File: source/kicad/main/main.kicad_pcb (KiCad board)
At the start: 4 copper layers, 50 x 50 mm, 108 parts

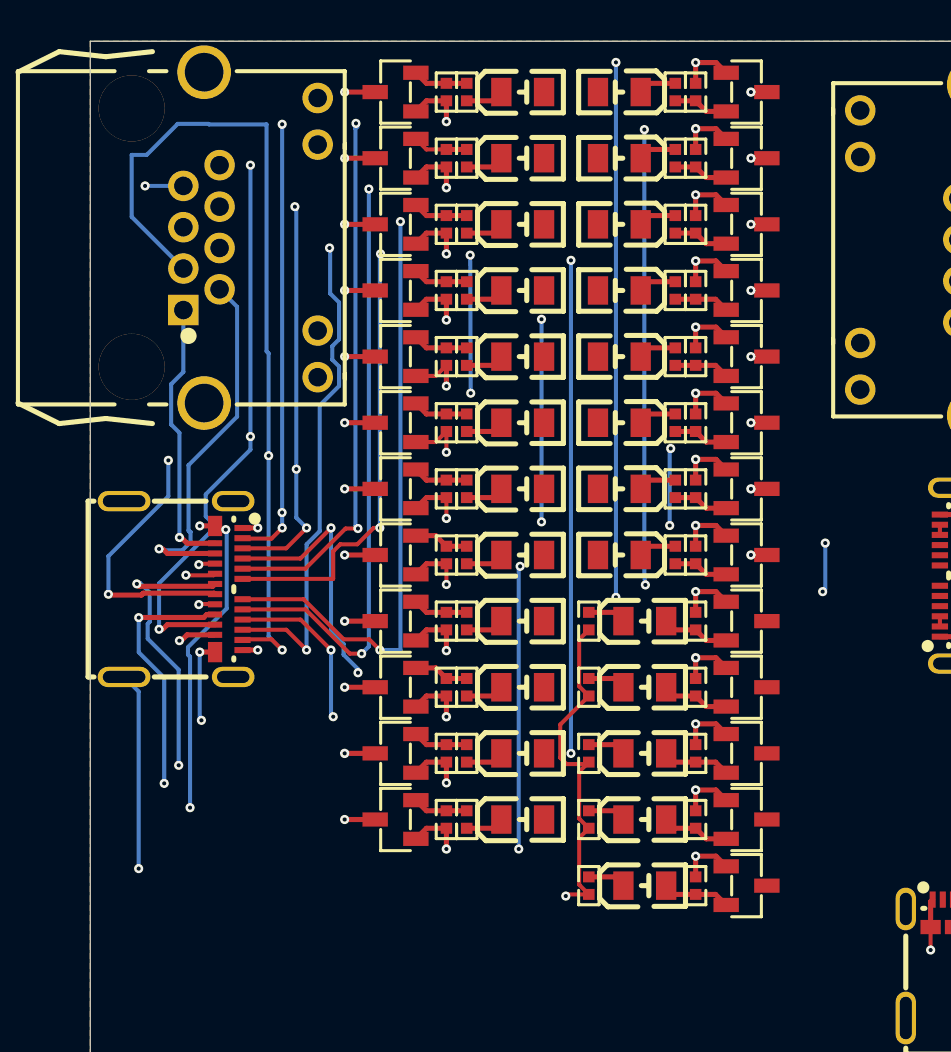
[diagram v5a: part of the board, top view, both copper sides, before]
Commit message: Bugfixes 1.0.0; WIP; Not exported yet.
- Fixed USB-C PD resistors
- Improved part-picking
- Fixed LedIndicator (wrong PowerSwitch usage)
- Reduced LED brightness
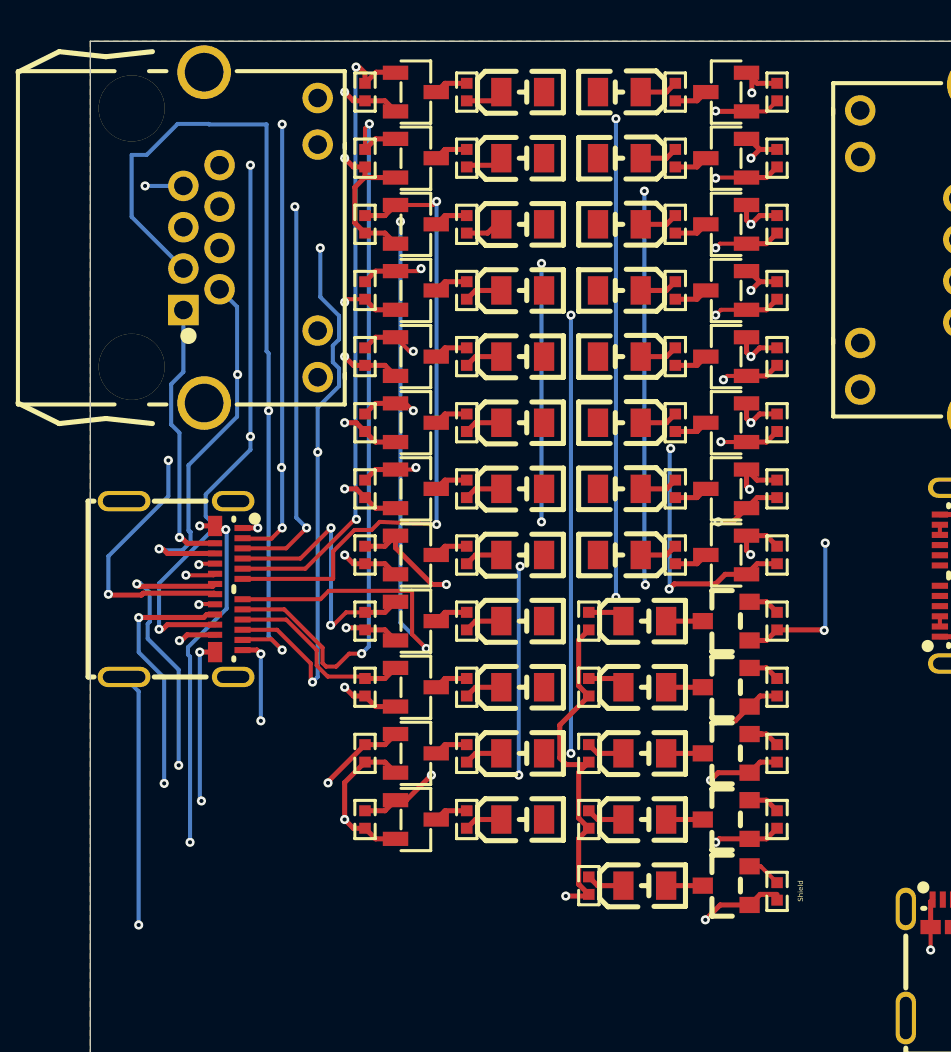
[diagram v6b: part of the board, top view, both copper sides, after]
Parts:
- removed tester.cc1.indicator.led.current_limiting_resistor[Resistor:300Ω], tester.cc2.indicator.led.current_limiting_resistor[Resistor:300Ω], tester.d1[0].indicator.led.current_limiting_resistor[Resistor:300Ω], tester.d1[1].indicator.led.current_limiting_resistor[Resistor:300Ω], tester.d2[0].indicator.led.current_limiting_resistor[Resistor:300Ω], tester.d2[1].indicator.led.current_limiting_resistor[Resistor:300Ω], tester.gnd[0].indicator.led.current_limiting_resistor[Resistor:300Ω], tester.gnd[1].indicator.led.current_limiting_resistor[Resistor:300Ω], tester.gnd[2].indicator.led.current_limiting_resistor[Resistor:300Ω], tester.gnd[3].indicator.led.current_limiting_resistor[Resistor:300Ω], tester.pair1_rx1[0].indicator.led.current_limiting_resistor[Resistor:300Ω], tester.pair1_rx1[1].indicator.led.current_limiting_resistor[Resistor:300Ω], tester.pair2_rx2[0].indicator.led.current_limiting_resistor[Resistor:300Ω], tester.pair2_rx2[1].indicator.led.current_limiting_resistor[Resistor:300Ω], tester.pair3_tx1[0].indicator.led.current_limiting_resistor[Resistor:300Ω], tester.pair3_tx1[1].indicator.led.current_limiting_resistor[Resistor:300Ω], tester.pair4_tx2[0].indicator.led.current_limiting_resistor[Resistor:300Ω], tester.pair4_tx2[1].indicator.led.current_limiting_resistor[Resistor:300Ω], tester.sbu1.indicator.led.current_limiting_resistor[Resistor:300Ω], tester.sbu2.indicator.led.current_limiting_resistor[Resistor:300Ω], tester.shield.indicator.led.current_limiting_resistor[Resistor:300Ω], tester.vbus[0].indicator.led.current_limiting_resistor[Resistor:300Ω], tester.vbus[1].indicator.led.current_limiting_resistor[Resistor:300Ω], tester.vbus[2].indicator.led.current_limiting_resistor[Resistor:300Ω], tester.vbus[3].indicator.led.current_limiting_resistor[Resistor:300Ω]: 300Ω, lcsc:R0402
- added tester.cc1.indicator.led.current_limiting_resistor[Resistor:1KΩ]: 1KΩ, lcsc:R0402, F.Cu at (18.5, 2.50)
- added tester.cc2.indicator.led.current_limiting_resistor[Resistor:1KΩ]: 1KΩ, lcsc:R0402, F.Cu at (28.8, 2.50)
- added tester.d1[0].indicator.led.current_limiting_resistor[Resistor:1KΩ]: 1KΩ, lcsc:R0402, F.Cu at (18.5, 9.00)
- added tester.d1[1].indicator.led.current_limiting_resistor[Resistor:1KΩ]: 1KΩ, lcsc:R0402, F.Cu at (28.8, 9.00)
- added tester.d2[0].indicator.led.current_limiting_resistor[Resistor:1KΩ]: 1KΩ, lcsc:R0402, F.Cu at (18.5, 12.2)
- added tester.d2[1].indicator.led.current_limiting_resistor[Resistor:1KΩ]: 1KΩ, lcsc:R0402, F.Cu at (28.8, 12.2)
- added tester.gnd[0].indicator.led.current_limiting_resistor[Resistor:1KΩ]: 1KΩ, lcsc:R0402, F.Cu at (24.5, 28.5)
- added tester.gnd[1].indicator.led.current_limiting_resistor[Resistor:1KΩ]: 1KΩ, lcsc:R0402, F.Cu at (24.5, 31.8)
- added tester.gnd[2].indicator.led.current_limiting_resistor[Resistor:1KΩ]: 1KΩ, lcsc:R0402, F.Cu at (24.5, 35.0)
- added tester.gnd[3].indicator.led.current_limiting_resistor[Resistor:1KΩ]: 1KΩ, lcsc:R0402, F.Cu at (24.5, 38.2)
- added tester.pair1_rx1[0].indicator.led.current_limiting_resistor[Resistor:1KΩ]: 1KΩ, lcsc:R0402, F.Cu at (18.5, 15.5)
- added tester.pair1_rx1[1].indicator.led.current_limiting_resistor[Resistor:1KΩ]: 1KΩ, lcsc:R0402, F.Cu at (28.8, 15.5)
- added tester.pair2_rx2[0].indicator.led.current_limiting_resistor[Resistor:1KΩ]: 1KΩ, lcsc:R0402, F.Cu at (18.5, 18.8)
- added tester.pair2_rx2[1].indicator.led.current_limiting_resistor[Resistor:1KΩ]: 1KΩ, lcsc:R0402, F.Cu at (28.8, 18.8)
- added tester.pair3_tx1[0].indicator.led.current_limiting_resistor[Resistor:1KΩ]: 1KΩ, lcsc:R0402, F.Cu at (18.5, 22.0)
- added tester.pair3_tx1[1].indicator.led.current_limiting_resistor[Resistor:1KΩ]: 1KΩ, lcsc:R0402, F.Cu at (28.8, 22.0)
- added tester.pair4_tx2[0].indicator.led.current_limiting_resistor[Resistor:1KΩ]: 1KΩ, lcsc:R0402, F.Cu at (18.5, 25.2)
- added tester.pair4_tx2[1].indicator.led.current_limiting_resistor[Resistor:1KΩ]: 1KΩ, lcsc:R0402, F.Cu at (28.8, 25.2)
- added tester.sbu1.indicator.led.current_limiting_resistor[Resistor:1KΩ]: 1KΩ, lcsc:R0402, F.Cu at (18.5, 5.75)
- added tester.sbu2.indicator.led.current_limiting_resistor[Resistor:1KΩ]: 1KΩ, lcsc:R0402, F.Cu at (28.8, 5.75)
- added tester.shield.indicator.led.current_limiting_resistor[Resistor:1KΩ]: 1KΩ, lcsc:R0402, F.Cu at (24.5, 41.5)
- added tester.vbus[0].indicator.led.current_limiting_resistor[Resistor:1KΩ]: 1KΩ, lcsc:R0402, F.Cu at (18.5, 28.5)
- added tester.vbus[1].indicator.led.current_limiting_resistor[Resistor:1KΩ]: 1KΩ, lcsc:R0402, F.Cu at (18.5, 31.8)
- added tester.vbus[2].indicator.led.current_limiting_resistor[Resistor:1KΩ]: 1KΩ, lcsc:R0402, F.Cu at (18.5, 35.0)
- added tester.vbus[3].indicator.led.current_limiting_resistor[Resistor:1KΩ]: 1KΩ, lcsc:R0402, F.Cu at (18.5, 38.2)
- tester.gnd[0].indicator.power_switch.mosfet[MOSFET:Q], tester.gnd[1].indicator.power_switch.mosfet[MOSFET:Q], tester.gnd[2].indicator.power_switch.mosfet[MOSFET:Q], tester.gnd[3].indicator.power_switch.mosfet[MOSFET:Q], tester.shield.indicator.power_switch.mosfet[MOSFET:Q]: footprint lcsc:SOT-23-3_L2.9-W1.3-P1.90-LS2.4-BR -> lcsc:SOT-23_L2.9-W1.3-P1.90-LS2.4-BR
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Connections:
- net psu.usb[USB_C_Receptacle:x]-psu.configuration_resistors[1][Resistor:5.0KΩ] renamed psu.configuration_resistors[1][Resistor:5.0KΩ]-psu.usb[USB_C_Receptacle:x]
- net tester.d1[0].indicator.power_switch[PowerSwitch:virt]-tester.d1[0][PairTester:virt]:4-tester.d1[0].i renamed tester.d1[0].indicator[LEDIndicator:virt]-tester.d1[0].indicator.power_switch[PowerSwitch:virt]-test
- net tester.d1[1].indicator.power_switch[PowerSwitch:virt]-tester.d1[1].indicator[LEDIndicator:virt]-test renamed tester.d1[1].indicator.power_switch[PowerSwitch:virt]-tester.d1[1][PairTester:virt]:4-tester.d1[1].i
- net tester.d2[0][PairTester:virt]:4-tester.d2[0].indicator.power_switch[PowerSwitch:virt]-tester.d2[0].i renamed tester.d2[0][PairTester:virt]:4-tester.d2[0].indicator[LEDIndicator:virt]-tester.d2[0].indicator.pow
- net tester.d2[1].indicator.power_switch[PowerSwitch:virt]-tester.d2[1][PairTester:virt]:4-tester.d2[1].i renamed tester.d2[1].indicator.power_switch[PowerSwitch:virt]-tester.d2[1].indicator[LEDIndicator:virt]-test
- net tester.gnd[0].indicator[LEDIndicator:virt]-tester.gnd[0][PairTester:virt]:4-tester.gnd[0].indicator. renamed tester.gnd[0][PairTester:virt]:4-tester.gnd[0].indicator[LEDIndicator:virt]-tester.gnd[0].indicator.
- net tester.gnd[1].indicator[LEDIndicator:virt]-tester.gnd[1][PairTester:virt]:4-tester.gnd[1].indicator. renamed tester.gnd[1][PairTester:virt]:4-tester.gnd[1].indicator.power_switch[PowerSwitch:virt]-tester.gnd[1
- net tester.gnd[2].indicator[LEDIndicator:virt]-tester.gnd[2][PairTester:virt]:4-tester.gnd[2].indicator. renamed tester.gnd[2][PairTester:virt]:4-tester.gnd[2].indicator.power_switch[PowerSwitch:virt]-tester.gnd[2
- net tester.gnd[3][PairTester:virt]:4-tester.gnd[3].indicator[LEDIndicator:virt]-tester.gnd[3].indicator. renamed tester.gnd[3][PairTester:virt]:4-tester.gnd[3].indicator.power_switch[PowerSwitch:virt]-tester.gnd[3
- net tester.pair2_rx2[0].indicator.power_switch[PowerSwitch:virt]-tester.pair2_rx2[0].indicator[LEDIndica renamed tester.pair2_rx2[0].indicator[LEDIndicator:virt]-tester.pair2_rx2[0].indicator.power_switch[PowerSwi
- net tester.pair3_tx1[0].indicator[LEDIndicator:virt]-tester.pair3_tx1[0][PairTester:virt]:4-tester.pair3 renamed tester.pair3_tx1[0].indicator[LEDIndicator:virt]-tester.pair3_tx1[0].indicator.power_switch[PowerSwi
- net tester.pair3_tx1[1].indicator[LEDIndicator:virt]-tester.pair3_tx1[1][PairTester:virt]:4-tester.pair3 renamed tester.pair3_tx1[1].indicator.power_switch[PowerSwitch:virt]-tester.pair3_tx1[1].indicator[LEDIndica
- net tester.pair4_tx2[0].indicator.power_switch[PowerSwitch:virt]-tester.pair4_tx2[0].indicator[LEDIndica renamed tester.pair4_tx2[0].indicator[LEDIndicator:virt]-tester.pair4_tx2[0][PairTester:virt]:4-tester.pair4
- net tester.pair4_tx2[1][PairTester:virt]:4-tester.pair4_tx2[1].indicator[LEDIndicator:virt]-tester.pair4 renamed tester.pair4_tx2[1].indicator[LEDIndicator:virt]-tester.pair4_tx2[1].indicator.power_switch[PowerSwi
- net tester.sbu1.indicator[LEDIndicator:virt]-tester.sbu1.indicator.power_switch[PowerSwitch:virt]-tester renamed tester.sbu1[PairTester:virt]:4-tester.sbu1.indicator[LEDIndicator:virt]-tester.sbu1.indicator.power_
- net tester.shield[PairTester:virt]:4-tester.shield.indicator[LEDIndicator:virt]-tester.shield.indicator. renamed tester.shield.indicator.power_switch[PowerSwitch:virt]-tester.shield[PairTester:virt]:4-tester.shiel
- net tester.vbus[0].indicator[LEDIndicator:virt]-tester.vbus[0][PairTester:virt]:4-tester.vbus[0].indicat renamed tester.vbus[0][PairTester:virt]:4-tester.vbus[0].indicator.power_switch[PowerSwitch:virt]-tester.vbu
- net tester.vbus[1].indicator.power_switch[PowerSwitch:virt]-tester.vbus[1][PairTester:virt]:4-tester.vbu renamed tester.vbus[1][PairTester:virt]:4-tester.vbus[1].indicator[LEDIndicator:virt]-tester.vbus[1].indicat
- net tester.vbus[3][PairTester:virt]:4-tester.vbus[3].indicator.power_switch[PowerSwitch:virt]-tester.vbu renamed tester.vbus[3].indicator[LEDIndicator:virt]-tester.vbus[3].indicator.power_switch[PowerSwitch:virt]-
- psu.configuration_resistors[0][Resistor:5.0KΩ] pad 2: tester.pair1_rx1[1][PairTester:virt]:2-tester.cc1[PairTester:virt]:2-tester.gnd[0].indicator.power_s -> tester.pair1_rx1[0][PairTester:virt]:2-tester.d1[1].indicator[LEDIndicator:virt]:3-tester.sbu2.indic
- psu.configuration_resistors[1][Resistor:5.0KΩ] pad 2: tester.pair1_rx1[1][PairTester:virt]:2-tester.cc1[PairTester:virt]:2-tester.gnd[0].indicator.power_s -> tester.pair1_rx1[0][PairTester:virt]:2-tester.d1[1].indicator[LEDIndicator:virt]:3-tester.sbu2.indic
- psu.usb[USB_C_Receptacle:x] pad A1: tester.pair1_rx1[1][PairTester:virt]:2-tester.cc1[PairTester:virt]:2-tester.gnd[0].indicator.power_s -> tester.pair1_rx1[0][PairTester:virt]:2-tester.d1[1].indicator[LEDIndicator:virt]:3-tester.sbu2.indic
- psu.usb[USB_C_Receptacle:x] pad A12: tester.pair1_rx1[1][PairTester:virt]:2-tester.cc1[PairTester:virt]:2-tester.gnd[0].indicator.power_s -> tester.pair1_rx1[0][PairTester:virt]:2-tester.d1[1].indicator[LEDIndicator:virt]:3-tester.sbu2.indic
- psu.usb[USB_C_Receptacle:x] pad A4: tester.d1[1].indicator.power_switch[PowerSwitch:virt]:4-tester.pair1_rx1[0].indicator.power_switch[P -> tester.shield.indicator.power_switch[PowerSwitch:virt]:2-tester.d1[1].indicator.power_switch[PowerSw
- psu.usb[USB_C_Receptacle:x] pad A9: tester.d1[1].indicator.power_switch[PowerSwitch:virt]:4-tester.pair1_rx1[0].indicator.power_switch[P -> tester.shield.indicator.power_switch[PowerSwitch:virt]:2-tester.d1[1].indicator.power_switch[PowerSw
- psu.usb[USB_C_Receptacle:x] pad B1: tester.pair1_rx1[1][PairTester:virt]:2-tester.cc1[PairTester:virt]:2-tester.gnd[0].indicator.power_s -> tester.pair1_rx1[0][PairTester:virt]:2-tester.d1[1].indicator[LEDIndicator:virt]:3-tester.sbu2.indic
- psu.usb[USB_C_Receptacle:x] pad B12: tester.pair1_rx1[1][PairTester:virt]:2-tester.cc1[PairTester:virt]:2-tester.gnd[0].indicator.power_s -> tester.pair1_rx1[0][PairTester:virt]:2-tester.d1[1].indicator[LEDIndicator:virt]:3-tester.sbu2.indic
- psu.usb[USB_C_Receptacle:x] pad B4: tester.d1[1].indicator.power_switch[PowerSwitch:virt]:4-tester.pair1_rx1[0].indicator.power_switch[P -> tester.shield.indicator.power_switch[PowerSwitch:virt]:2-tester.d1[1].indicator.power_switch[PowerSw
- psu.usb[USB_C_Receptacle:x] pad B9: tester.d1[1].indicator.power_switch[PowerSwitch:virt]:4-tester.pair1_rx1[0].indicator.power_switch[P -> tester.shield.indicator.power_switch[PowerSwitch:virt]:2-tester.d1[1].indicator.power_switch[PowerSw
- tester.cc1.indicator.led.led[LED:D] pad 1: tester.d1[1].indicator.power_switch[PowerSwitch:virt]:4-tester.pair1_rx1[0].indicator.power_switch[P -> tester.shield.indicator.power_switch[PowerSwitch:virt]:2-tester.d1[1].indicator.power_switch[PowerSw
- tester.cc1.indicator.led.led[LED:D] pad 2: tester.cc1.indicator.led.led[LED:D]-tester.cc1.indicator.led.current_limiting_resistor[Resistor:300Ω] -> tester.cc1.indicator.led.current_limiting_resistor[Resistor:1KΩ]-tester.cc1.indicator.led.led[LED:D]
- tester.cc1.indicator.power_switch.mosfet[MOSFET:Q] pad 2: tester.cc1.indicator.led[PoweredLED:virt]:2-tester.cc1.indicator.power_switch[PowerSwitch:virt]:3 -> tester.pair1_rx1[0][PairTester:virt]:2-tester.d1[1].indicator[LEDIndicator:virt]:3-tester.sbu2.indic
- tester.cc1.indicator.power_switch.mosfet[MOSFET:Q] pad 3: tester.pair1_rx1[1][PairTester:virt]:2-tester.cc1[PairTester:virt]:2-tester.gnd[0].indicator.power_s -> tester.cc1.indicator.led[PoweredLED:virt]:2-tester.cc1.indicator.power_switch[PowerSwitch:virt]:5
- tester.cc1.indicator.power_switch.pull_resistor[Resistor:100KΩ] pad 2: tester.cc1.indicator.led[PoweredLED:virt]:2-tester.cc1.indicator.power_switch[PowerSwitch:virt]:3 -> tester.pair1_rx1[0][PairTester:virt]:2-tester.d1[1].indicator[LEDIndicator:virt]:3-tester.sbu2.indic
- tester.cc2.indicator.led.led[LED:D] pad 1: tester.d1[1].indicator.power_switch[PowerSwitch:virt]:4-tester.pair1_rx1[0].indicator.power_switch[P -> tester.shield.indicator.power_switch[PowerSwitch:virt]:2-tester.d1[1].indicator.power_switch[PowerSw
- tester.cc2.indicator.led.led[LED:D] pad 2: tester.cc2.indicator.led.current_limiting_resistor[Resistor:300Ω]-tester.cc2.indicator.led.led[LED:D] -> tester.cc2.indicator.led.current_limiting_resistor[Resistor:1KΩ]-tester.cc2.indicator.led.led[LED:D]
- tester.cc2.indicator.power_switch.mosfet[MOSFET:Q] pad 2: tester.cc2.indicator.power_switch[PowerSwitch:virt]:3-tester.cc2.indicator.led[PoweredLED:virt]:2 -> tester.pair1_rx1[0][PairTester:virt]:2-tester.d1[1].indicator[LEDIndicator:virt]:3-tester.sbu2.indic
- tester.cc2.indicator.power_switch.mosfet[MOSFET:Q] pad 3: tester.pair1_rx1[1][PairTester:virt]:2-tester.cc1[PairTester:virt]:2-tester.gnd[0].indicator.power_s -> tester.cc2.indicator.led[PoweredLED:virt]:2-tester.cc2.indicator.power_switch[PowerSwitch:virt]:5
- tester.cc2.indicator.power_switch.pull_resistor[Resistor:100KΩ] pad 2: tester.cc2.indicator.power_switch[PowerSwitch:virt]:3-tester.cc2.indicator.led[PoweredLED:virt]:2 -> tester.pair1_rx1[0][PairTester:virt]:2-tester.d1[1].indicator[LEDIndicator:virt]:3-tester.sbu2.indic
- tester.d1[0].indicator.led.led[LED:D] pad 1: tester.d1[1].indicator.power_switch[PowerSwitch:virt]:4-tester.pair1_rx1[0].indicator.power_switch[P -> tester.shield.indicator.power_switch[PowerSwitch:virt]:2-tester.d1[1].indicator.power_switch[PowerSw
- tester.d1[0].indicator.led.led[LED:D] pad 2: tester.d1[0].indicator.led.led[LED:D]-tester.d1[0].indicator.led.current_limiting_resistor[Resistor:300Ω] -> tester.d1[0].indicator.led.led[LED:D]-tester.d1[0].indicator.led.current_limiting_resistor[Resistor:1KΩ]
- tester.d1[0].indicator.power_switch.mosfet[MOSFET:Q] pad 2: tester.d1[0].indicator.led[PoweredLED:virt]:2-tester.d1[0].indicator.power_switch[PowerSwitch:virt]: -> tester.pair1_rx1[0][PairTester:virt]:2-tester.d1[1].indicator[LEDIndicator:virt]:3-tester.sbu2.indic
- tester.d1[0].indicator.power_switch.mosfet[MOSFET:Q] pad 3: tester.pair1_rx1[1][PairTester:virt]:2-tester.cc1[PairTester:virt]:2-tester.gnd[0].indicator.power_s -> tester.d1[0].indicator.power_switch[PowerSwitch:virt]:5-tester.d1[0].indicator.led[PoweredLED:virt]:
- tester.d1[0].indicator.power_switch.pull_resistor[Resistor:100KΩ] pad 2: tester.d1[0].indicator.led[PoweredLED:virt]:2-tester.d1[0].indicator.power_switch[PowerSwitch:virt]: -> tester.pair1_rx1[0][PairTester:virt]:2-tester.d1[1].indicator[LEDIndicator:virt]:3-tester.sbu2.indic
- tester.d1[1].indicator.led.led[LED:D] pad 1: tester.d1[1].indicator.power_switch[PowerSwitch:virt]:4-tester.pair1_rx1[0].indicator.power_switch[P -> tester.shield.indicator.power_switch[PowerSwitch:virt]:2-tester.d1[1].indicator.power_switch[PowerSw
- tester.d1[1].indicator.led.led[LED:D] pad 2: tester.d1[1].indicator.led.current_limiting_resistor[Resistor:300Ω]-tester.d1[1].indicator.led.led[LED:D] -> tester.d1[1].indicator.led.current_limiting_resistor[Resistor:1KΩ]-tester.d1[1].indicator.led.led[LED:D]
- tester.d1[1].indicator.power_switch.mosfet[MOSFET:Q] pad 2: tester.d1[1].indicator.led[PoweredLED:virt]:2-tester.d1[1].indicator.power_switch[PowerSwitch:virt]: -> tester.pair1_rx1[0][PairTester:virt]:2-tester.d1[1].indicator[LEDIndicator:virt]:3-tester.sbu2.indic
- tester.d1[1].indicator.power_switch.mosfet[MOSFET:Q] pad 3: tester.pair1_rx1[1][PairTester:virt]:2-tester.cc1[PairTester:virt]:2-tester.gnd[0].indicator.power_s -> tester.d1[1].indicator.power_switch[PowerSwitch:virt]:5-tester.d1[1].indicator.led[PoweredLED:virt]:
- tester.d1[1].indicator.power_switch.pull_resistor[Resistor:100KΩ] pad 2: tester.d1[1].indicator.led[PoweredLED:virt]:2-tester.d1[1].indicator.power_switch[PowerSwitch:virt]: -> tester.pair1_rx1[0][PairTester:virt]:2-tester.d1[1].indicator[LEDIndicator:virt]:3-tester.sbu2.indic
- tester.d2[0].indicator.led.led[LED:D] pad 1: tester.d1[1].indicator.power_switch[PowerSwitch:virt]:4-tester.pair1_rx1[0].indicator.power_switch[P -> tester.shield.indicator.power_switch[PowerSwitch:virt]:2-tester.d1[1].indicator.power_switch[PowerSw
- tester.d2[0].indicator.led.led[LED:D] pad 2: tester.d2[0].indicator.led.current_limiting_resistor[Resistor:300Ω]-tester.d2[0].indicator.led.led[LED:D] -> tester.d2[0].indicator.led.led[LED:D]-tester.d2[0].indicator.led.current_limiting_resistor[Resistor:1KΩ]
- tester.d2[0].indicator.power_switch.mosfet[MOSFET:Q] pad 2: tester.d2[0].indicator.led[PoweredLED:virt]:2-tester.d2[0].indicator.power_switch[PowerSwitch:virt]: -> tester.pair1_rx1[0][PairTester:virt]:2-tester.d1[1].indicator[LEDIndicator:virt]:3-tester.sbu2.indic
- tester.d2[0].indicator.power_switch.mosfet[MOSFET:Q] pad 3: tester.pair1_rx1[1][PairTester:virt]:2-tester.cc1[PairTester:virt]:2-tester.gnd[0].indicator.power_s -> tester.d2[0].indicator.led[PoweredLED:virt]:2-tester.d2[0].indicator.power_switch[PowerSwitch:virt]:
- tester.d2[0].indicator.power_switch.pull_resistor[Resistor:100KΩ] pad 2: tester.d2[0].indicator.led[PoweredLED:virt]:2-tester.d2[0].indicator.power_switch[PowerSwitch:virt]: -> tester.pair1_rx1[0][PairTester:virt]:2-tester.d1[1].indicator[LEDIndicator:virt]:3-tester.sbu2.indic
- tester.d2[1].indicator.led.led[LED:D] pad 1: tester.d1[1].indicator.power_switch[PowerSwitch:virt]:4-tester.pair1_rx1[0].indicator.power_switch[P -> tester.shield.indicator.power_switch[PowerSwitch:virt]:2-tester.d1[1].indicator.power_switch[PowerSw
- tester.d2[1].indicator.led.led[LED:D] pad 2: tester.d2[1].indicator.led.current_limiting_resistor[Resistor:300Ω]-tester.d2[1].indicator.led.led[LED:D] -> tester.d2[1].indicator.led.current_limiting_resistor[Resistor:1KΩ]-tester.d2[1].indicator.led.led[LED:D]
- tester.d2[1].indicator.power_switch.mosfet[MOSFET:Q] pad 2: tester.d2[1].indicator.led[PoweredLED:virt]:2-tester.d2[1].indicator.power_switch[PowerSwitch:virt]: -> tester.pair1_rx1[0][PairTester:virt]:2-tester.d1[1].indicator[LEDIndicator:virt]:3-tester.sbu2.indic
- tester.d2[1].indicator.power_switch.mosfet[MOSFET:Q] pad 3: tester.pair1_rx1[1][PairTester:virt]:2-tester.cc1[PairTester:virt]:2-tester.gnd[0].indicator.power_s -> tester.d2[1].indicator.led[PoweredLED:virt]:2-tester.d2[1].indicator.power_switch[PowerSwitch:virt]:
- tester.d2[1].indicator.power_switch.pull_resistor[Resistor:100KΩ] pad 2: tester.d2[1].indicator.led[PoweredLED:virt]:2-tester.d2[1].indicator.power_switch[PowerSwitch:virt]: -> tester.pair1_rx1[0][PairTester:virt]:2-tester.d1[1].indicator[LEDIndicator:virt]:3-tester.sbu2.indic
- tester.gnd[0].indicator.led.led[LED:D] pad 2: tester.gnd[0].indicator.led.led[LED:D]-tester.gnd[0].indicator.led.current_limiting_resistor[Resistor:300Ω] -> tester.gnd[0].indicator.led.current_limiting_resistor[Resistor:1KΩ]-tester.gnd[0].indicator.led.led[LED:D]
- tester.gnd[0].indicator.power_switch.mosfet[MOSFET:Q] pad 2: tester.gnd[0].indicator.led[PoweredLED:virt]-tester.gnd[0].indicator.power_switch[PowerSwitch:virt]: -> tester.shield.indicator.power_switch[PowerSwitch:virt]:2-tester.d1[1].indicator.power_switch[PowerSw
- tester.gnd[0].indicator.power_switch.mosfet[MOSFET:Q] pad 3: tester.d1[1].indicator.power_switch[PowerSwitch:virt]:4-tester.pair1_rx1[0].indicator.power_switch[P -> tester.gnd[0].indicator.led[PoweredLED:virt]-tester.gnd[0].indicator.power_switch[PowerSwitch:virt]:
- tester.gnd[0].indicator.power_switch.pull_resistor[Resistor:100KΩ] pad 2: tester.gnd[0].indicator.led[PoweredLED:virt]-tester.gnd[0].indicator.power_switch[PowerSwitch:virt]: -> tester.shield.indicator.power_switch[PowerSwitch:virt]:2-tester.d1[1].indicator.power_switch[PowerSw
- tester.gnd[1].indicator.led.led[LED:D] pad 1: tester.gnd[1].indicator.power_switch[PowerSwitch:virt]:2-tester.gnd[1].indicator.led[PoweredLED:virt -> tester.gnd[1].indicator.led[PoweredLED:virt]-tester.gnd[1].indicator.power_switch[PowerSwitch:virt]:
- tester.gnd[1].indicator.led.led[LED:D] pad 2: tester.gnd[1].indicator.led.current_limiting_resistor[Resistor:300Ω]-tester.gnd[1].indicator.led.led[LED:D] -> tester.gnd[1].indicator.led.led[LED:D]-tester.gnd[1].indicator.led.current_limiting_resistor[Resistor:1KΩ]
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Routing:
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- added copper zone on F.Cu, net tester.shield.indicator.power_switch[PowerSwitch:virt]:2-tester.d1[1].indicator.power_switch[PowerSw
- removed copper zone on F.Cu, net tester.d1[1].indicator.power_switch[PowerSwitch:virt]:4-tester.pair1_rx1[0].indicator.power_switch[P
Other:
- board text added: "Shield"
- board text added: "USB-C CableTester v1.0.1 https://github.com/IoannisP-ITENG/CableTester"
- board text removed: "USB-C CableTester v1.0.0 https://github.com/IoannisP-ITENG/CableTester"

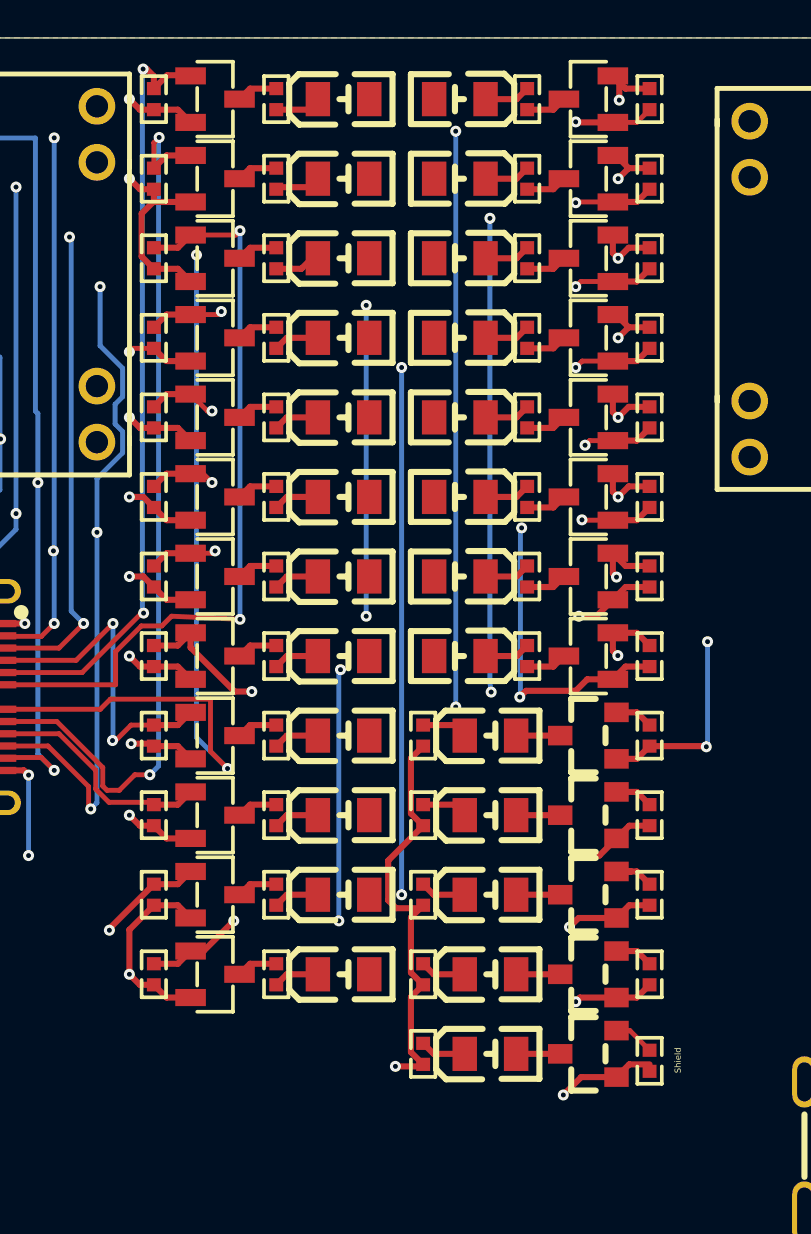
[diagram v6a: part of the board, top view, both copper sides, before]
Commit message: Fix footprints/3dmodels
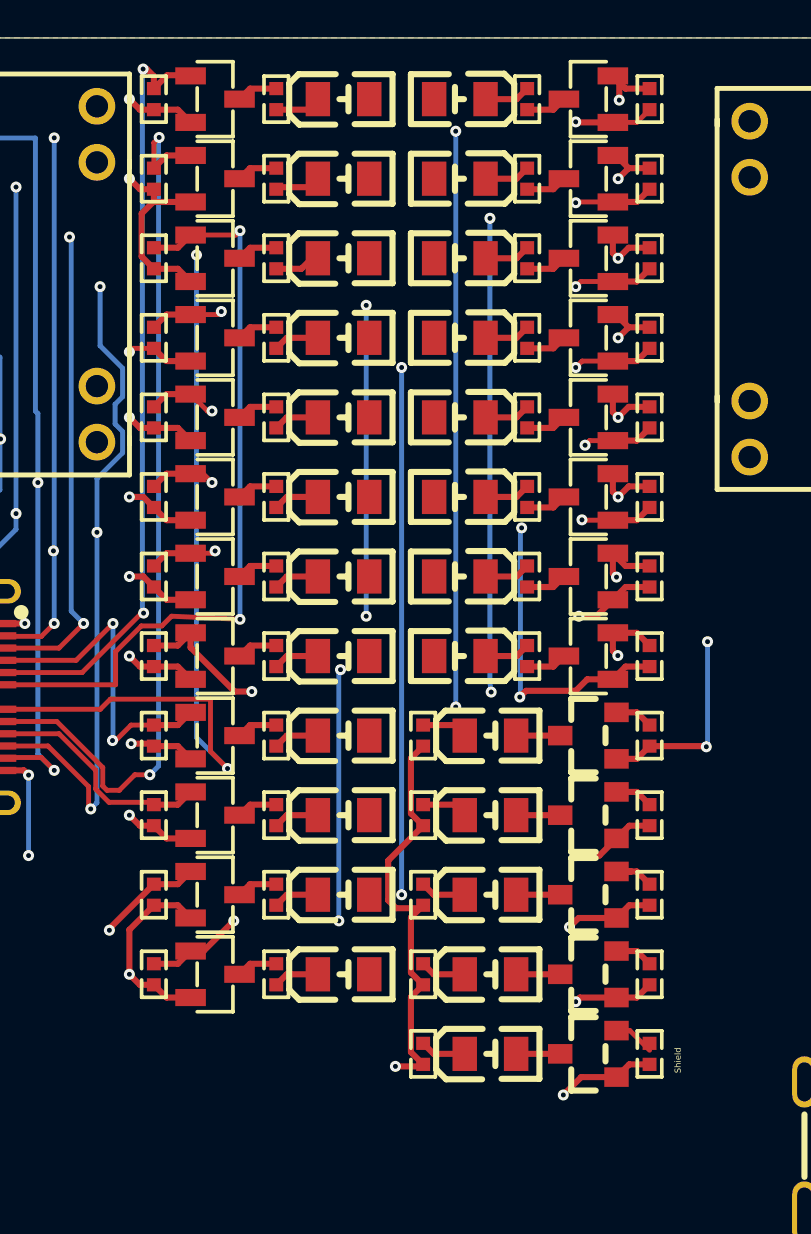
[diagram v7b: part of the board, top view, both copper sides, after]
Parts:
- moved tester.shield.indicator.power_switch.pull_resistor[Resistor:100KΩ] 0.28 mm to (33.8, 41.5)
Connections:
- net psu.configuration_resistors[0][Resistor:5.0KΩ]-psu.usb[USB_C_Receptacle:x] renamed psu.usb[USB_C_Receptacle:x]-psu.configuration_resistors[0][Resistor:5.0KΩ]
- net psu.configuration_resistors[1][Resistor:5.0KΩ]-psu.usb[USB_C_Receptacle:x] renamed psu.usb[USB_C_Receptacle:x]-psu.configuration_resistors[1][Resistor:5.0KΩ]
- net tester.cc1.indicator.led[PoweredLED:virt]:2-tester.cc1.indicator.power_switch[PowerSwitch:virt]:5 renamed tester.cc1.indicator.power_switch[PowerSwitch:virt]:5-tester.cc1.indicator.led[PoweredLED:virt]:2
- net tester.cc1[PairTester:virt]:4-tester.cc1.indicator[LEDIndicator:virt]-tester.cc1.indicator.power_swi renamed tester.cc1.indicator[LEDIndicator:virt]-tester.cc1.indicator.power_switch[PowerSwitch:virt]-tester.c
- net tester.cc2.indicator.led.current_limiting_resistor[Resistor:1KΩ]-tester.cc2.indicator.led.led[LED:D] renamed tester.cc2.indicator.led.led[LED:D]-tester.cc2.indicator.led.current_limiting_resistor[Resistor:1KΩ]
- net tester.cc2.indicator.led[PoweredLED:virt]:2-tester.cc2.indicator.power_switch[PowerSwitch:virt]:5 renamed tester.cc2.indicator.power_switch[PowerSwitch:virt]:5-tester.cc2.indicator.led[PoweredLED:virt]:2
- net tester.cc2[PairTester:virt]:4-tester.cc2.indicator.power_switch[PowerSwitch:virt]-tester.cc2.indicat renamed tester.cc2.indicator.power_switch[PowerSwitch:virt]-tester.cc2.indicator[LEDIndicator:virt]-tester.c
- net tester.d1[0].indicator.led.led[LED:D]-tester.d1[0].indicator.led.current_limiting_resistor[Resistor:1KΩ] renamed tester.d1[0].indicator.led.current_limiting_resistor[Resistor:1KΩ]-tester.d1[0].indicator.led.led[LED:D]
- net tester.d1[0].indicator.power_switch[PowerSwitch:virt]:5-tester.d1[0].indicator.led[PoweredLED:virt]: renamed tester.d1[0].indicator.led[PoweredLED:virt]:2-tester.d1[0].indicator.power_switch[PowerSwitch:virt]:
- net tester.d1[1].indicator.led.current_limiting_resistor[Resistor:1KΩ]-tester.d1[1].indicator.led.led[LED:D] renamed tester.d1[1].indicator.led.led[LED:D]-tester.d1[1].indicator.led.current_limiting_resistor[Resistor:1KΩ]
- net tester.d2[0].indicator.led.led[LED:D]-tester.d2[0].indicator.led.current_limiting_resistor[Resistor:1KΩ] renamed tester.d2[0].indicator.led.current_limiting_resistor[Resistor:1KΩ]-tester.d2[0].indicator.led.led[LED:D]
- net tester.d2[0].indicator.led[PoweredLED:virt]:2-tester.d2[0].indicator.power_switch[PowerSwitch:virt]: renamed tester.d2[0].indicator.power_switch[PowerSwitch:virt]:5-tester.d2[0].indicator.led[PoweredLED:virt]:
- net tester.d2[0][PairTester:virt]:4-tester.d2[0].indicator[LEDIndicator:virt]-tester.d2[0].indicator.pow renamed tester.d2[0][PairTester:virt]:4-tester.d2[0].indicator.power_switch[PowerSwitch:virt]-tester.d2[0].i
- net tester.d2[1].indicator.led[PoweredLED:virt]:2-tester.d2[1].indicator.power_switch[PowerSwitch:virt]: renamed tester.d2[1].indicator.power_switch[PowerSwitch:virt]:5-tester.d2[1].indicator.led[PoweredLED:virt]:
- net tester.d2[1].indicator.power_switch[PowerSwitch:virt]-tester.d2[1].indicator[LEDIndicator:virt]-test renamed tester.d2[1][PairTester:virt]:4-tester.d2[1].indicator[LEDIndicator:virt]-tester.d2[1].indicator.pow
- net tester.gnd[0].indicator.led.current_limiting_resistor[Resistor:1KΩ]-tester.gnd[0].indicator.led.led[LED:D] renamed tester.gnd[0].indicator.led.led[LED:D]-tester.gnd[0].indicator.led.current_limiting_resistor[Resistor:1KΩ]
- net tester.gnd[0].indicator.led[PoweredLED:virt]-tester.gnd[0].indicator.power_switch[PowerSwitch:virt]: renamed tester.gnd[0].indicator.power_switch[PowerSwitch:virt]:4-tester.gnd[0].indicator.led[PoweredLED:virt
- net tester.gnd[0][PairTester:virt]:4-tester.gnd[0].indicator[LEDIndicator:virt]-tester.gnd[0].indicator. renamed tester.gnd[0].indicator.power_switch[PowerSwitch:virt]-tester.gnd[0].indicator[LEDIndicator:virt]-te
- net tester.gnd[1].indicator.led[PoweredLED:virt]-tester.gnd[1].indicator.power_switch[PowerSwitch:virt]: renamed tester.gnd[1].indicator.power_switch[PowerSwitch:virt]:4-tester.gnd[1].indicator.led[PoweredLED:virt
- net tester.gnd[2][PairTester:virt]:4-tester.gnd[2].indicator.power_switch[PowerSwitch:virt]-tester.gnd[2 renamed tester.gnd[2][PairTester:virt]:4-tester.gnd[2].indicator[LEDIndicator:virt]-tester.gnd[2].indicator.
- net tester.gnd[3].indicator.led.current_limiting_resistor[Resistor:1KΩ]-tester.gnd[3].indicator.led.led[LED:D] renamed tester.gnd[3].indicator.led.led[LED:D]-tester.gnd[3].indicator.led.current_limiting_resistor[Resistor:1KΩ]
- net tester.gnd[3].indicator.power_switch[PowerSwitch:virt]:4-tester.gnd[3].indicator.led[PoweredLED:virt renamed tester.gnd[3].indicator.led[PoweredLED:virt]-tester.gnd[3].indicator.power_switch[PowerSwitch:virt]:
- net tester.gnd[3][PairTester:virt]:4-tester.gnd[3].indicator.power_switch[PowerSwitch:virt]-tester.gnd[3 renamed tester.gnd[3][PairTester:virt]:4-tester.gnd[3].indicator[LEDIndicator:virt]-tester.gnd[3].indicator.
- net tester.pair1_rx1[0].indicator.led.current_limiting_resistor[Resistor:1KΩ]-tester.pair1_rx1[0].indicator.led.led[LED:D] renamed tester.pair1_rx1[0].indicator.led.led[LED:D]-tester.pair1_rx1[0].indicator.led.current_limiting_resistor[Resistor:1KΩ]
- net tester.pair1_rx1[0].indicator.power_switch[PowerSwitch:virt]:5-tester.pair1_rx1[0].indicator.led[Pow renamed tester.pair1_rx1[0].indicator.led[PoweredLED:virt]:2-tester.pair1_rx1[0].indicator.power_switch[Powe
- net tester.pair1_rx1[0].indicator[LEDIndicator:virt]-tester.pair1_rx1[0][PairTester:virt]:4-tester.pair1 renamed tester.pair1_rx1[0][PairTester:virt]:4-tester.pair1_rx1[0].indicator.power_switch[PowerSwitch:virt]-
- net tester.pair1_rx1[0][PairTester:virt]:2-tester.d1[1].indicator[LEDIndicator:virt]:3-tester.sbu2.indic renamed tester.vbus[1].indicator[LEDIndicator:virt]:3-tester.shield.indicator[LEDIndicator:virt]:3-tester.gn
- net tester.pair1_rx1[1][PairTester:virt]:4-tester.pair1_rx1[1].indicator.power_switch[PowerSwitch:virt]- renamed tester.pair1_rx1[1][PairTester:virt]:4-tester.pair1_rx1[1].indicator[LEDIndicator:virt]-tester.pair1
- net tester.pair2_rx2[0].indicator[LEDIndicator:virt]-tester.pair2_rx2[0].indicator.power_switch[PowerSwi renamed tester.pair2_rx2[0].indicator[LEDIndicator:virt]-tester.pair2_rx2[0][PairTester:virt]:4-tester.pair2
- net tester.pair2_rx2[1].indicator[LEDIndicator:virt]-tester.pair2_rx2[1][PairTester:virt]:4-tester.pair2 renamed tester.pair2_rx2[1].indicator.power_switch[PowerSwitch:virt]-tester.pair2_rx2[1].indicator[LEDIndica
- net tester.pair3_tx1[0].indicator.led[PoweredLED:virt]:2-tester.pair3_tx1[0].indicator.power_switch[Powe renamed tester.pair3_tx1[0].indicator.power_switch[PowerSwitch:virt]:5-tester.pair3_tx1[0].indicator.led[Pow
- net tester.pair3_tx1[0].indicator[LEDIndicator:virt]-tester.pair3_tx1[0].indicator.power_switch[PowerSwi renamed tester.pair3_tx1[0].indicator.power_switch[PowerSwitch:virt]-tester.pair3_tx1[0][PairTester:virt]:4-
- net tester.pair3_tx1[1].indicator.led[PoweredLED:virt]:2-tester.pair3_tx1[1].indicator.power_switch[Powe renamed tester.pair3_tx1[1].indicator.power_switch[PowerSwitch:virt]:5-tester.pair3_tx1[1].indicator.led[Pow
- net tester.pair3_tx1[1].indicator.power_switch[PowerSwitch:virt]-tester.pair3_tx1[1].indicator[LEDIndica renamed tester.pair3_tx1[1].indicator[LEDIndicator:virt]-tester.pair3_tx1[1][PairTester:virt]:4-tester.pair3
- net tester.pair4_tx2[0].indicator[LEDIndicator:virt]-tester.pair4_tx2[0][PairTester:virt]:4-tester.pair4 renamed tester.pair4_tx2[0].indicator[LEDIndicator:virt]-tester.pair4_tx2[0].indicator.power_switch[PowerSwi
- net tester.pair4_tx2[1].indicator.led.current_limiting_resistor[Resistor:1KΩ]-tester.pair4_tx2[1].indicator.led.led[LED:D] renamed tester.pair4_tx2[1].indicator.led.led[LED:D]-tester.pair4_tx2[1].indicator.led.current_limiting_resistor[Resistor:1KΩ]
- net tester.pair4_tx2[1].indicator.led[PoweredLED:virt]:2-tester.pair4_tx2[1].indicator.power_switch[Powe renamed tester.pair4_tx2[1].indicator.power_switch[PowerSwitch:virt]:5-tester.pair4_tx2[1].indicator.led[Pow
- net tester.sbu1[PairTester:virt]:4-tester.sbu1.indicator[LEDIndicator:virt]-tester.sbu1.indicator.power_ renamed tester.sbu1.indicator[LEDIndicator:virt]-tester.sbu1.indicator.power_switch[PowerSwitch:virt]-tester
- net tester.sbu2.indicator.led.current_limiting_resistor[Resistor:1KΩ]-tester.sbu2.indicator.led.led[LED:D] renamed tester.sbu2.indicator.led.led[LED:D]-tester.sbu2.indicator.led.current_limiting_resistor[Resistor:1KΩ]
- net tester.sbu2.indicator.led[PoweredLED:virt]:2-tester.sbu2.indicator.power_switch[PowerSwitch:virt]:5 renamed tester.sbu2.indicator.power_switch[PowerSwitch:virt]:5-tester.sbu2.indicator.led[PoweredLED:virt]:2
- net tester.sbu2[PairTester:virt]:4-tester.sbu2.indicator.power_switch[PowerSwitch:virt]-tester.sbu2.indi renamed tester.sbu2.indicator.power_switch[PowerSwitch:virt]-tester.sbu2[PairTester:virt]:4-tester.sbu2.indi
- net tester.shield.indicator.led.current_limiting_resistor[Resistor:1KΩ]-tester.shield.indicator.led.led[LED:D] renamed tester.shield.indicator.led.led[LED:D]-tester.shield.indicator.led.current_limiting_resistor[Resistor:1KΩ]
- net tester.shield.indicator.power_switch[PowerSwitch:virt]-tester.shield[PairTester:virt]:4-tester.shiel renamed tester.shield.indicator.power_switch[PowerSwitch:virt]-tester.shield.indicator[LEDIndicator:virt]-te
- net tester.shield.indicator.power_switch[PowerSwitch:virt]:2-tester.d1[1].indicator.power_switch[PowerSw renamed tester.pair1_rx1[1].indicator.led[PoweredLED:virt]-tester.d2[1].indicator.power_switch[PowerSwitch:v
- net tester.shield.indicator.power_switch[PowerSwitch:virt]:4-tester.shield.indicator.led[PoweredLED:virt renamed tester.shield.indicator.led[PoweredLED:virt]-tester.shield.indicator.power_switch[PowerSwitch:virt]:
- net tester.vbus[0].indicator.led.current_limiting_resistor[Resistor:1KΩ]-tester.vbus[0].indicator.led.led[LED:D] renamed tester.vbus[0].indicator.led.led[LED:D]-tester.vbus[0].indicator.led.current_limiting_resistor[Resistor:1KΩ]
- net tester.vbus[0][PairTester:virt]:4-tester.vbus[0].indicator.power_switch[PowerSwitch:virt]-tester.vbu renamed tester.vbus[0][PairTester:virt]:4-tester.vbus[0].indicator[LEDIndicator:virt]-tester.vbus[0].indicat
- net tester.vbus[1].indicator.led.current_limiting_resistor[Resistor:1KΩ]-tester.vbus[1].indicator.led.led[LED:D] renamed tester.vbus[1].indicator.led.led[LED:D]-tester.vbus[1].indicator.led.current_limiting_resistor[Resistor:1KΩ]
- net tester.vbus[1][PairTester:virt]:4-tester.vbus[1].indicator[LEDIndicator:virt]-tester.vbus[1].indicat renamed tester.vbus[1][PairTester:virt]:4-tester.vbus[1].indicator.power_switch[PowerSwitch:virt]-tester.vbu
- net tester.vbus[2].indicator.led.current_limiting_resistor[Resistor:1KΩ]-tester.vbus[2].indicator.led.led[LED:D] renamed tester.vbus[2].indicator.led.led[LED:D]-tester.vbus[2].indicator.led.current_limiting_resistor[Resistor:1KΩ]
- net tester.vbus[2].indicator.power_switch[PowerSwitch:virt]:5-tester.vbus[2].indicator.led[PoweredLED:vi renamed tester.vbus[2].indicator.led[PoweredLED:virt]:2-tester.vbus[2].indicator.power_switch[PowerSwitch:vi
- net tester.vbus[3].indicator.led.led[LED:D]-tester.vbus[3].indicator.led.current_limiting_resistor[Resistor:1KΩ] renamed tester.vbus[3].indicator.led.current_limiting_resistor[Resistor:1KΩ]-tester.vbus[3].indicator.led.led[LED:D]
- net tester.vbus[3].indicator.led[PoweredLED:virt]:2-tester.vbus[3].indicator.power_switch[PowerSwitch:vi renamed tester.vbus[3].indicator.power_switch[PowerSwitch:virt]:5-tester.vbus[3].indicator.led[PoweredLED:vi
- net tester.vbus[3].indicator[LEDIndicator:virt]-tester.vbus[3].indicator.power_switch[PowerSwitch:virt]- renamed tester.vbus[3][PairTester:virt]:4-tester.vbus[3].indicator.power_switch[PowerSwitch:virt]-tester.vbu
